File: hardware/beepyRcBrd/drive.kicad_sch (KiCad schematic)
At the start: 17 parts, among them J1 Conn_01x06, J10 Conn_01x03, J11 Conn_01x03, J2 Conn_01x06, J5 Conn_01x06, J6 Conn_01x06, J9 Conn_01x03, U1 TC118S, U6 TC118S, U7 TC118S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

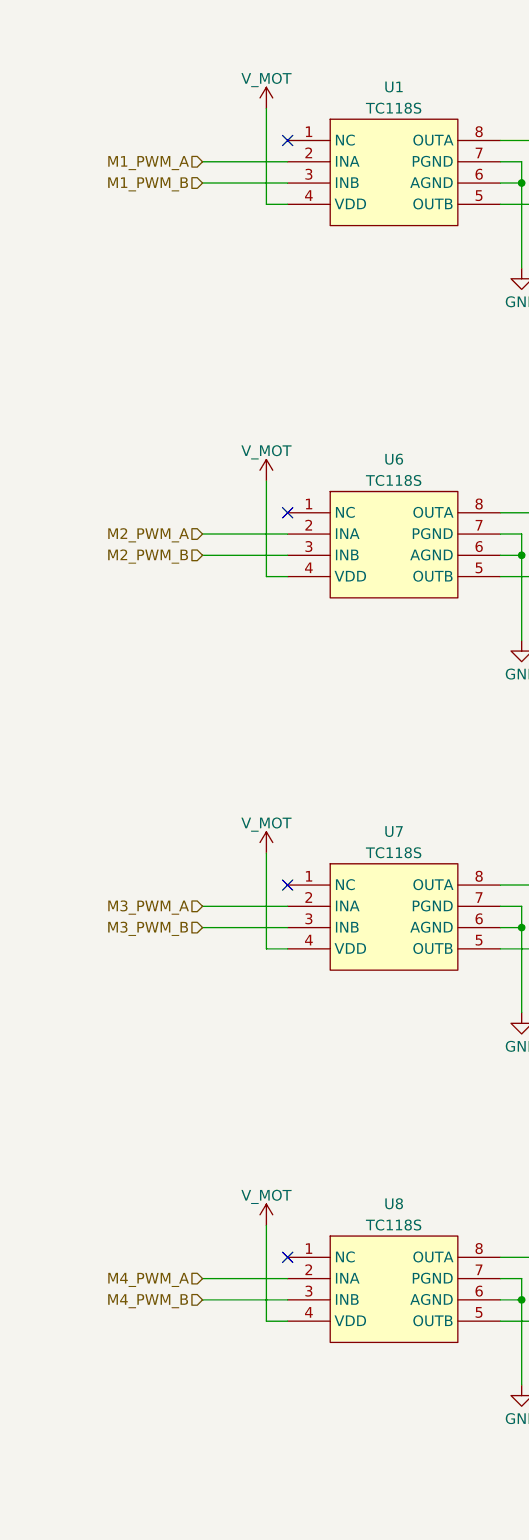
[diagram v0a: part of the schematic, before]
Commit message: fix: motor PWM pulled down
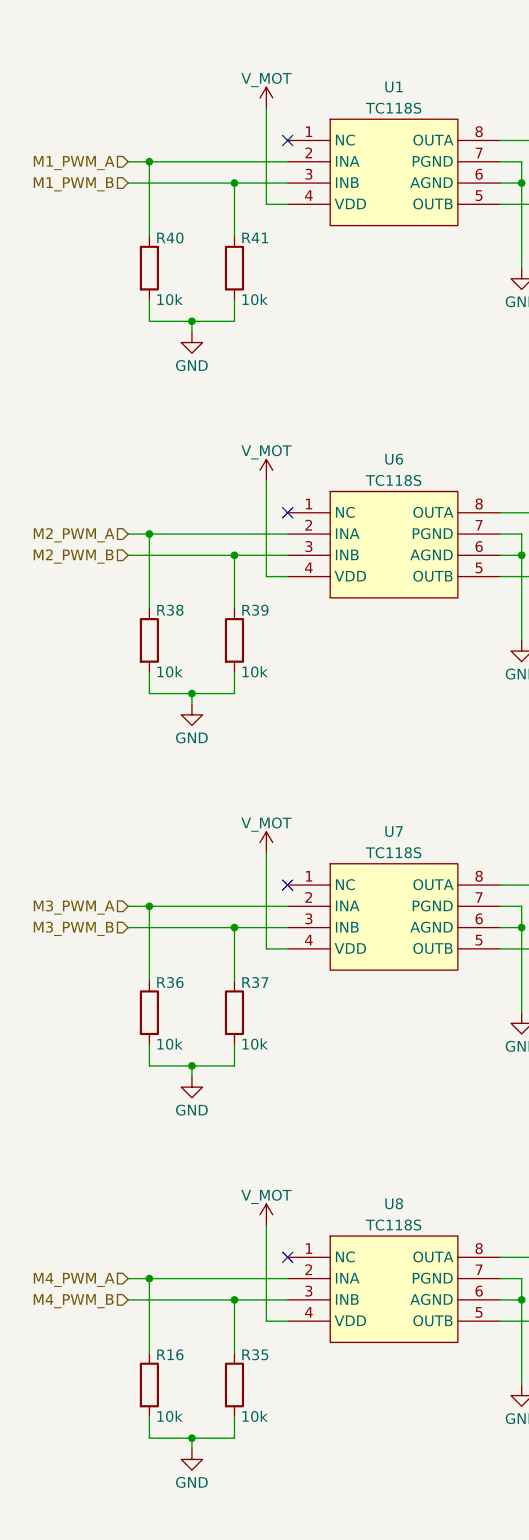
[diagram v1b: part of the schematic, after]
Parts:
- added R16, R35, R36, R37, R38, R39, R40, R41: 10k, Resistor_SMD:R_0603_1608Metric_Pad0.98x0.95mm_HandSolder, symbol beepyRc_symbols:R
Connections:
- net GND: now also R16.2, R35.2, R36.2, R37.2, R38.2, R39.2, R40.2, R41.2
- net M1_PWM_A: now also R40.1
- net M1_PWM_B: now also R41.1
- net M2_PWM_A: now also R38.1
- net M2_PWM_B: now also R39.1
- net M3_PWM_A: now also R36.1
- net M3_PWM_B: now also R37.1
- net M4_PWM_A: now also R16.1
- net M4_PWM_B: now also R35.1

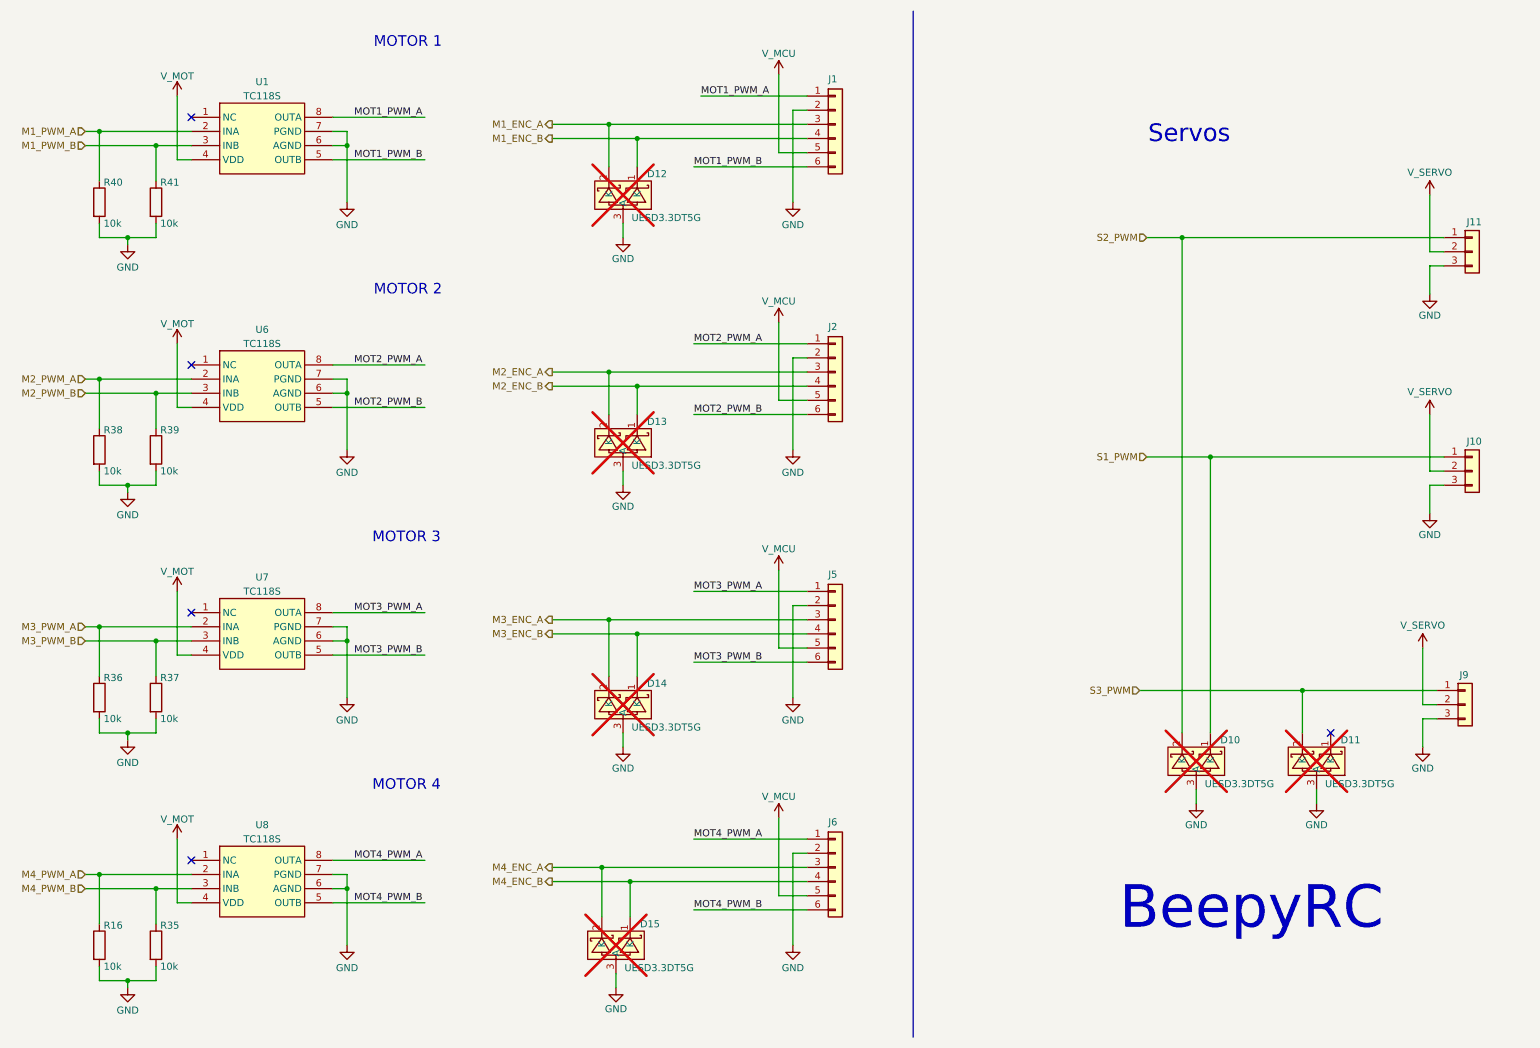
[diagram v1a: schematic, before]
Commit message: fix: passing schematics ERC rules
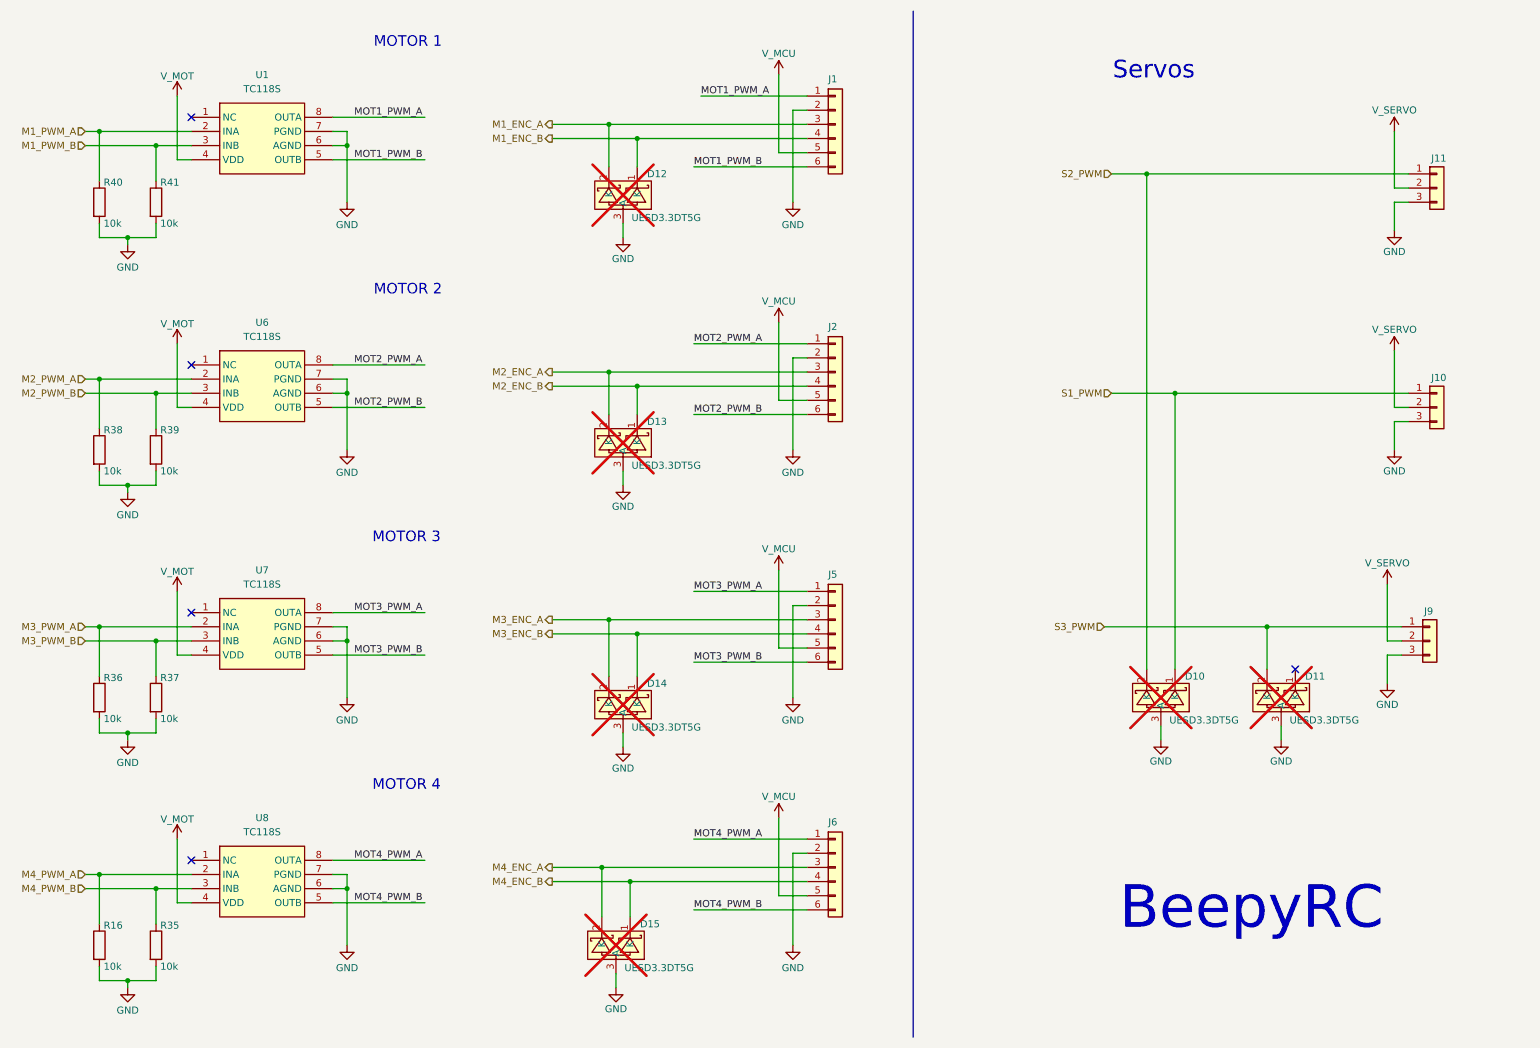
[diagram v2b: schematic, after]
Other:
- moved on the sheet: D10, D11, J11

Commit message: feat: completed beepyRcBrd_rev_0_0.pdf
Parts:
- added H10, H11, H12, H5, H6, H7, H8, H9: MT, beepyRcBrd:MountingHole_2.2mm_M2_DIN965_Pad_TopBottom, symbol beepyRc_symbols:MountingHole_Pad
- D10, D11, D12, D13, D14, D15: footprint lscs:SOT-723_L1.2-W0.8-P0.40-LS1.2-BR -> beepyRcBrd:SOT-723_L1.2-W0.8-P0.40-LS1.2-BR
- J1, J2, J5, J6: footprint TestPoint:TestPoint_Bridge_Pitch2.54mm_Drill1.0mm -> beepyRcBrd:PinHeader_1x06_P2.54mm_Vertical
- J10, J11, J9: footprint TestPoint:TestPoint_Bridge_Pitch2.54mm_Drill1.0mm -> beepyRcBrd:PinHeader_1x03_P2.54mm_Vertical
- R16, R35, R36, R37, R38, R39, R40, R41: footprint Resistor_SMD:R_0603_1608Metric_Pad0.98x0.95mm_HandSolder -> beepyRcBrd:R_0603_1608Metric_Pad0.98x0.95mm_HandSolder
- U1, U6, U7, U8: footprint lscs:SOP-8_L4.9-W3.9-P1.27-LS6.0-BL -> beepyRcBrd:SOP-8_L4.9-W3.9-P1.27-LS6.0-BL
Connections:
- net GND: now also H10.1, H11.1, H12.1, H5.1, H6.1, H7.1, H8.1, H9.1
- net M2_ENC_A: now also D13.1 (K); no longer D13.2 (K)
- net M2_ENC_B: now also D13.2 (K); no longer D13.1 (K)
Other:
- note added: "Motor Mounting Holes"
- moved on the sheet: D10, D11, J10, J11, J9
